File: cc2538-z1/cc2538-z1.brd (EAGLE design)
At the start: 56.8 x 35.6 mm, 61 parts, among them Q2 DMG6602SVT, U1 CC2538, U2 CC1120_RHM_32, U3 TPD2E001IDRLRQ1, U4 CP2103, X1 FA-128, X2 32MHz

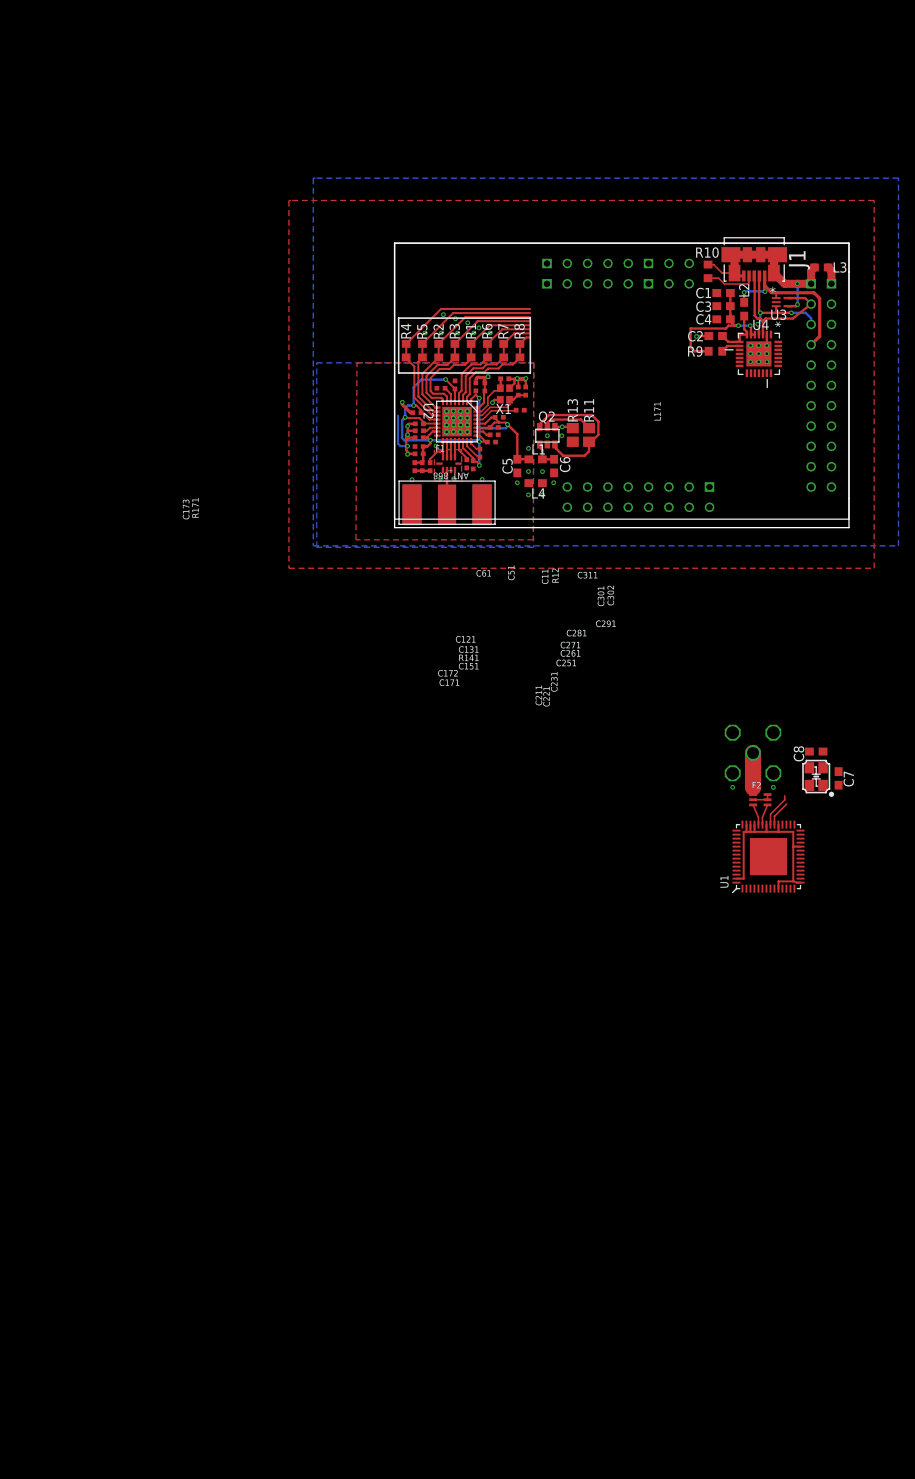
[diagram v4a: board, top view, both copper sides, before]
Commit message: Board check in before placing & routing CPU
Added CC1120/1200 ref chunk

Added partslist with Farnell links
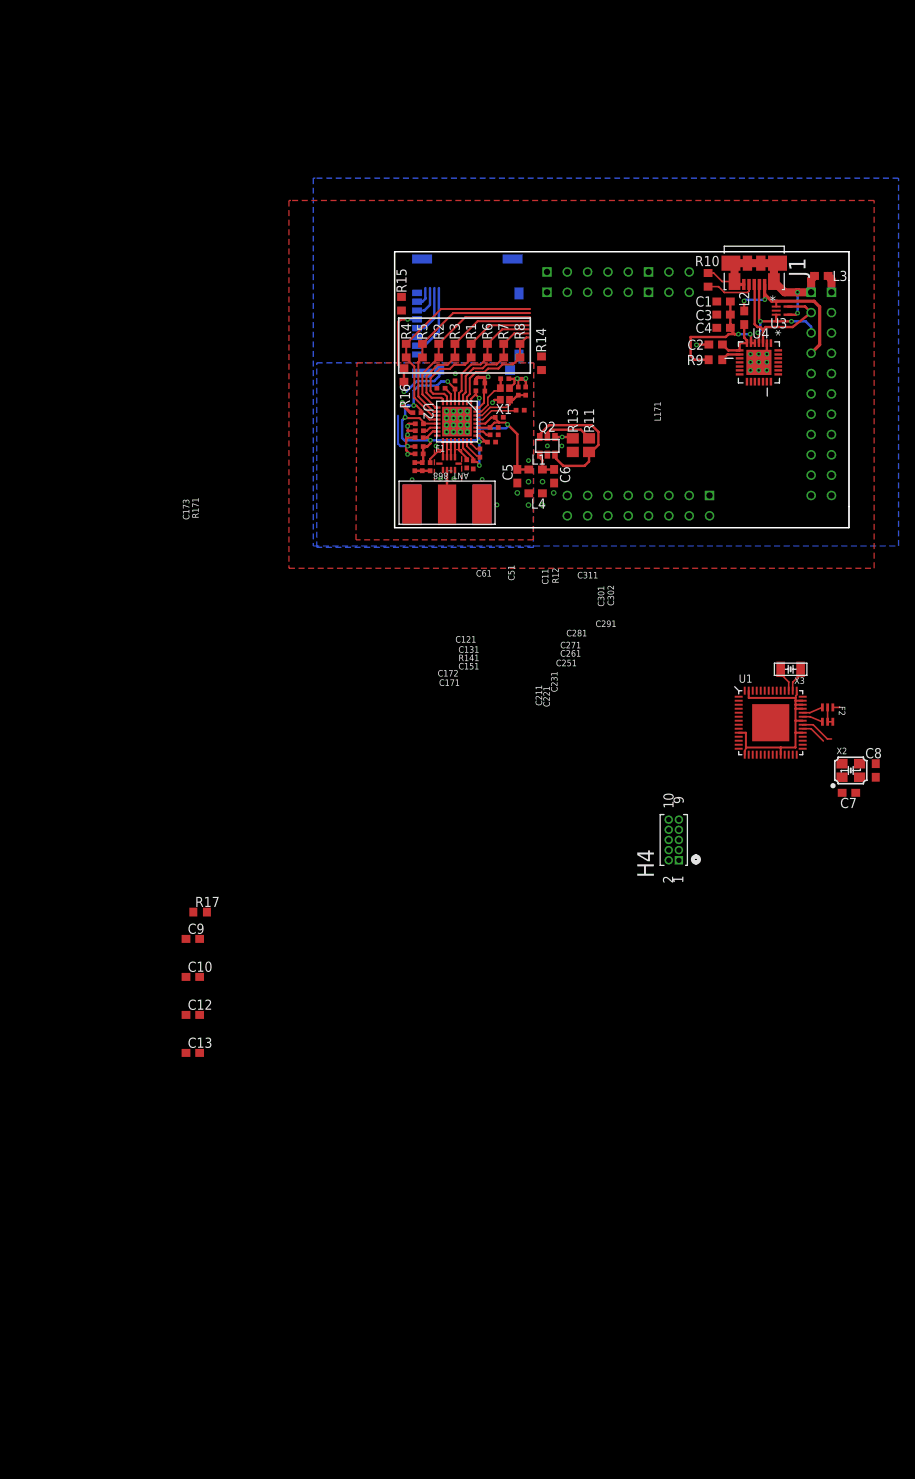
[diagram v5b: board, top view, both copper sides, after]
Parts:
- removed U$1: SMATH, CC11x:SMA
- added C10, C9: 1uF, rcl:C0603
- added C12, C13: 47p, rcl:C0603
- added H4: FTS-105-01-L-D, CC11x:SAMTEC_FTS-105-01-L-D
- added R14: 100k, rcl:R0603
- added R15: DNP, rcl:R0603
- added R16: (no value), rcl:R0603
- added R17: 56k, rcl:R0603
- added SD1: MICRO_SD-SPI-MOLEX_503182-0853, glacsweb:MICRO_SD-MOLEX_503182-0853
- added X3: 32.768K, arm-cores:XTAL-3.2X1.5
- R9: value 4.7k -> 10k
- moved U1 16.7 mm to (47.0, -24.4), turned to 0 degrees
- moved F2 13.6 mm to (54.1, -23.4), turned to 0 degrees
- moved C8 7.81 mm to (60.1, -30.4), turned to 90 degrees
- moved X2 4.38 mm to (57.0, -30.4), turned to 0 degrees
- moved C7 2.22 mm to (56.8, -33.1), turned to 180 degrees
- moved C5 1.27 mm to (15.3, 6.43)
- moved C6 1.27 mm to (19.9, 6.43)
- moved L1 1.27 mm to (17.6, 7.26)
- moved L4 1.27 mm to (17.6, 4.29)
- moved Q2 1.27 mm to (20.4, 9.42)
- moved R11 1.27 mm to (24.3, 10.3)
- moved R13 1.27 mm to (22.3, 10.3)
- moved H1 1.06 mm to (1.27, 34.5)
- moved J1 1.06 mm to (45.0, 30.4)
- moved R10 1.06 mm to (39.2, 31.0)
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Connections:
- removed net ADC_1: H1.A16
- removed net ADC_2: H1.A9
- removed net ADC_BATVOLTS: H1.A6
- removed net I2C_INT: U1.26
- removed net N$22: U1.27
- removed net N$23: U1.20
- removed net N$24: H1.C44
- removed net N$25: H1.C41
- removed net N$32: H1.B29
- removed net N$33: H1.B27
- removed net N$39: H1.A15
- removed net N$42: H1.A5
- removed net N$43: H1.A7
- removed net N$45: H1.A8
- removed net N$49: H1.C52
- removed net N$50: H1.C50
- removed net N$54: H1.C54
- removed net N$56: H1.C45
- removed net N$60: H1.C53
- removed net N$61: H1.C47
- removed net N$69: U1.49
- removed net N$71: U1.48
- new net 32K_Q1: C12.2, U1.45, X3.2
- new net 32K_Q2: C13.2, U1.44, X3.1
- new net ADC_SENSORS_ADC2: H1.A9, U1.20
- new net CC2538_NRESET: H4.10, U1.28
- new net DCOUPL: C10.2, C9.2, U1.32, U1.56
- new net JTAG_TCK: H4.4, U1.47
- new net JTAG_TDI: H4.8
- new net JTAG_TMS: H4.2, H4.6, U1.46
- net +3V3: now also H4.1, R15.2, SD1.DETECT, U1.43
- net 2.4G: no longer U$1.SIG
- net ADC_SENSORS_ADC1: now also H1.A16
- net ADC_SENSORS_ADC3: now also H1.A6
- net DIGITAL_IO_1: now also U1.48
- net DIGITAL_IO_2: now also U1.49
- net GND: now also C10.1, C12.1, C13.1, C9.1, H4.3, H4.5, R14.2, R17.2, SD1.6; no longer U$1.GND1, U$1.GND2, U$1.GND3, U$1.GND4
- net N$21: now also R17.1, U1.42; no longer U1.25
- net PWR_RADIO_EN: now also U1.27
- net PWR_SENSE_EN: now also U1.26
- net RADIO_GPIO2: now also H1.C42
- net RADIO_GPIO3: no longer H1.C42
- net RS485_TXEN: now also U1.25
- net SD_SEL: now also R14.1, R15.1, R16.1, R16.2, SD1.4, SD1.SWITCH
- net SD_SPI_CLK: now also SD1.5
- net SD_SPI_CSN: now also SD1.2
- net SD_SPI_MISO: now also SD1.7
- net SD_SPI_MOSI: now also SD1.3
- net UART0_RX: now also H1.C47
- net UART0_TX: now also H1.C53
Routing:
- net SD_SEL: track 0.00 -> 17.9 mm, vias 0 -> 2
- net SD_SPI_MISO: track 0.00 -> 8.90 mm
- net SD_SPI_CLK: track 0.00 -> 6.46 mm
- net 2.4G: track 5.21 -> 0.86 mm
- net SD_SPI_MOSI: track 0.00 -> 4.01 mm
- net 32K_Q1: track 0.00 -> 3.10 mm
- net 32K_Q2: track 0.00 -> 3.09 mm
- net SD_SPI_CSN: track 0.00 -> 2.53 mm
- net RGND: track 30.1 -> 31.9 mm, vias 18 -> 20
- net RVDD: track 75.8 -> 76.9 mm
- net +3V3: track 34.6 -> 35.6 mm
- net GND: vias 26 -> 15
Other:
- board size 56.8 x 35.6 mm -> 56.8 x 34.5 mm

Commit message: PCB routing attempt 1
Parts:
- added ANT: UFL, CC11x:UFL-HIROSE
- added C14, C15: 1uF, CC11x:C0603
- added J2: 2-PIN-MOLEX, farnell-parts:2-MOLEX
- added LED: (no value), CC11x:PLCC-4_3.2X2.8
- added R18, R19: 100k, rcl:R0603
- added R20, R21, R22: 220, rcl:R0603
- added R23, R24, R25: 4.7K, rcl:R0603
- added R26, R27: 4.7k, rcl:R0603
- added RST, USR: (no value), CC11x:C&K-KMR-5MM
- added U5, U6, U7: BSS138PS, CC11x:SOT65P210X110-6N
- R7: value (none) -> 220
- moved R7 137.6 mm to (-46.0, -101.9), turned to 0 degrees
- moved C13 107.3 mm to (35.6, 22.8), turned to 270 degrees
- moved C12 102.0 mm to (33.2, 22.8), turned to 270 degrees
- moved R17 90.7 mm to (39.3, 16.6)
- moved H4 60.5 mm to (25.3, 23.3), turned to 180 degrees
- moved X2 42.6 mm to (40.5, 8.89)
- moved C7 42.6 mm to (40.3, 6.10)
- moved C8 42.6 mm to (43.6, 8.89)
- moved X3 40.8 mm to (34.4, 20.1)
- moved F2 39.8 mm to (39.0, 13.5)
- moved U1 39.8 mm to (31.9, 12.4)
- moved R11 4.20 mm to (21.3, 13.3), turned to 180 degrees
- moved R8 2.05 mm to (13.6, 21.9)
- moved R14 0.97 mm to (17.5, 20.1), turned to 0 degrees
- moved R9 0.38 mm to (40.1, 21.4)
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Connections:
- removed net DIGITAL_IO_1: H1.C51, U1.48
- removed net DIGITAL_IO_2: H1.A10, U1.49
- removed net JTAG_TDI: H4.8
- new net JTAG_TDI/DIO2: H1.A10, H4.8, U1.49
- new net JTAG_TDO/DIO1: H1.C51, H4.6, U1.48
- new net N$22: LED.1, R20.2
- new net N$23: LED.3, R21.2
- new net N$24: LED.4, R22.2
- new net N$25: R20.1, U5.6
- new net N$32: R21.1, U6.6
- new net N$33: R22.1, U5.3
- net +3V3: now also J2.1, J2.2, LED.2, R18.2, R19.2
- net 2.4G: now also ANT.RF
- net BSL_DTR: now also R27.2, U7.2
- net BSL_RTS: now also R26.2, U7.5
- net CC2538_NRESET: now also C14.1, R18.1, RST.1, RST.5, U7.3
- net GND: now also ANT.1, ANT.2, C14.2, C15.2, H4.9, R23.2, R24.2, R25.2, R26.1, R27.1, RST.2, RST.3, RST.4, U5.1, U5.4, U6.1, U7.1, U7.4, USR.2, USR.3, USR.4
- net JTAG_TMS: no longer H4.6
- net LEDS_BLUE: now also R25.1, U6.2
- net LEDS_GREEN: now also R24.1, U5.5
- net LEDS_RED: now also R23.1, U5.2
- net RADIO_GPIO3: no longer R7.1, R7.2
- net USER_BUTTON: now also C15.1, R19.1, U7.6, USR.1, USR.5
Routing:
- net UART0_TX: track 0.00 -> 52.5 mm, vias 0 -> 3
- net UART0_RX: track 0.00 -> 46.3 mm, vias 0 -> 2
- net USER_BUTTON: track 0.00 -> 38.8 mm
- net CC2538_NRESET: track 0.00 -> 23.2 mm
- net RADIO_SPI_CSN: track 28.2 -> 49.7 mm, vias 0 -> 1
- net RADIO_GPIO0: track 25.0 -> 45.6 mm, vias 0 -> 1
- net RADIO_SPI_MISO: track 22.8 -> 42.8 mm, vias 0 -> 1
- net RADIO_SPI_CLK: track 21.6 -> 40.9 mm, vias 0 -> 1
- net RADIO_RESET_N: track 13.7 -> 33.0 mm
- net RADIO_SPI_MOSI: track 20.9 -> 39.6 mm, vias 0 -> 1
- net RADIO_GPIO2: track 15.5 -> 34.0 mm
- net SD_SPI_CSN: track 2.53 -> 20.8 mm
- net SD_SPI_MOSI: track 4.01 -> 20.7 mm
- net BSL_DTR: track 0.00 -> 16.6 mm, vias 0 -> 2
- net RADIO_GPIO3: track 14.6 -> 0.00 mm
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
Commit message: 48 airwires left.
Still need to finalise SD sel setup.

May need to swap to a 4-layer board.

What am I doing working on PCBs at 8 am?
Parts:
- removed R7: 220, rcl:R0603
- moved R19 102.7 mm to (43.2, -2.29)
- moved R18 92.4 mm to (54.8, 1.45)
- moved C10 89.7 mm to (24.8, 18.3)
- moved C9 84.6 mm to (36.4, 6.53), turned to 90 degrees
- moved R25 42.9 mm to (-23.6, -79.8), turned to 180 degrees
- moved R24 35.2 mm to (-23.6, -84.3), turned to 180 degrees
- moved R23 33.3 mm to (-23.6, -82.0), turned to 180 degrees
- moved X3 2.30 mm to (34.1, 22.4)
- moved C12 2.30 mm to (32.9, 25.0)
- moved C13 2.30 mm to (35.4, 25.0)
- moved C8 1.80 mm to (42.4, 10.2)
- moved F2 1.80 mm to (37.7, 14.7)
- moved R17 1.80 mm to (38.0, 17.9)
- moved U1 1.80 mm to (30.6, 13.7)
- moved ANT 1.80 mm to (41.3, 15.6)
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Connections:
- net RADIO_GPIO0: now also H1.C54
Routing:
- net PWR_RADIO_EN: track 2.90 -> 49.7 mm, vias 1 -> 3
- net RADIO_SPI_MISO: track 42.8 -> 86.8 mm, vias 1 -> 2
- net RADIO_SPI_MOSI: track 39.6 -> 78.4 mm, vias 1 -> 2
- net I2C_SCL: track 0.00 -> 37.4 mm, vias 0 -> 2
- net I2C_SDA: track 0.00 -> 37.1 mm, vias 0 -> 2
- net RADIO_SPI_CLK: track 40.9 -> 75.1 mm, vias 1 -> 2
- net PWR_SENSE_EN: track 0.00 -> 31.4 mm, vias 0 -> 2
- net UART1_RX: track 0.00 -> 30.3 mm, vias 0 -> 1
- net UART1_TX: track 0.00 -> 27.6 mm, vias 0 -> 1
- net DCOUPL: track 0.00 -> 24.1 mm, vias 0 -> 2
- net SD_SPI_CLK: track 20.9 -> 43.8 mm, vias 0 -> 1
- net SD_SPI_MOSI: track 20.7 -> 42.1 mm, vias 0 -> 1
- net SD_SPI_MISO: track 22.6 -> 43.5 mm, vias 0 -> 1
- net JTAG_TCK: track 0.00 -> 8.13 mm
- net JTAG_TMS: track 0.00 -> 7.29 mm
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
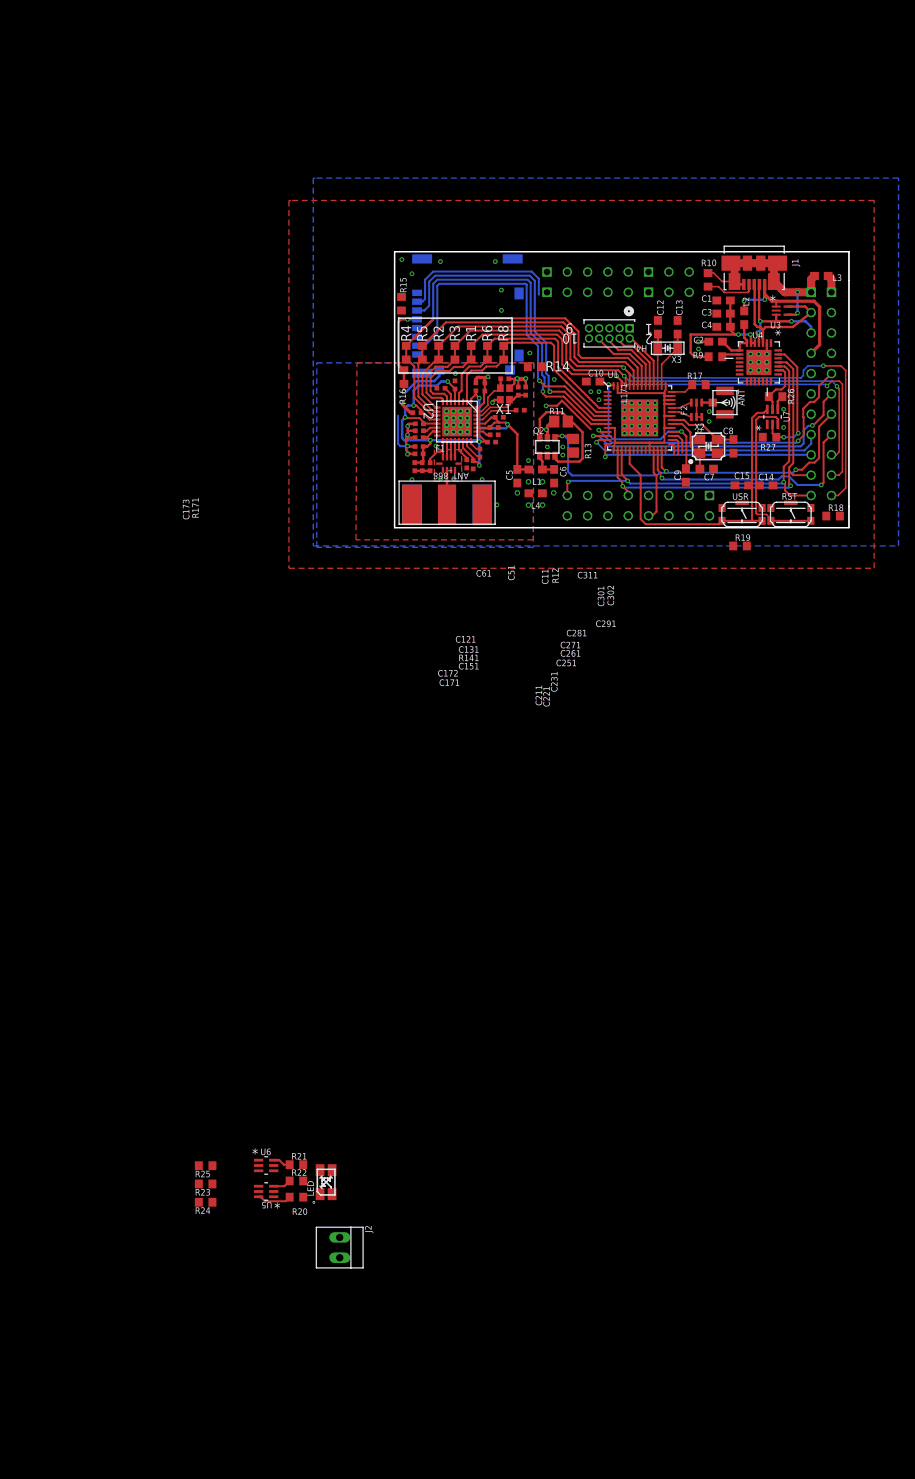
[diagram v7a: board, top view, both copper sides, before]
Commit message: Last commit before going 4-layer for cc2538 board.
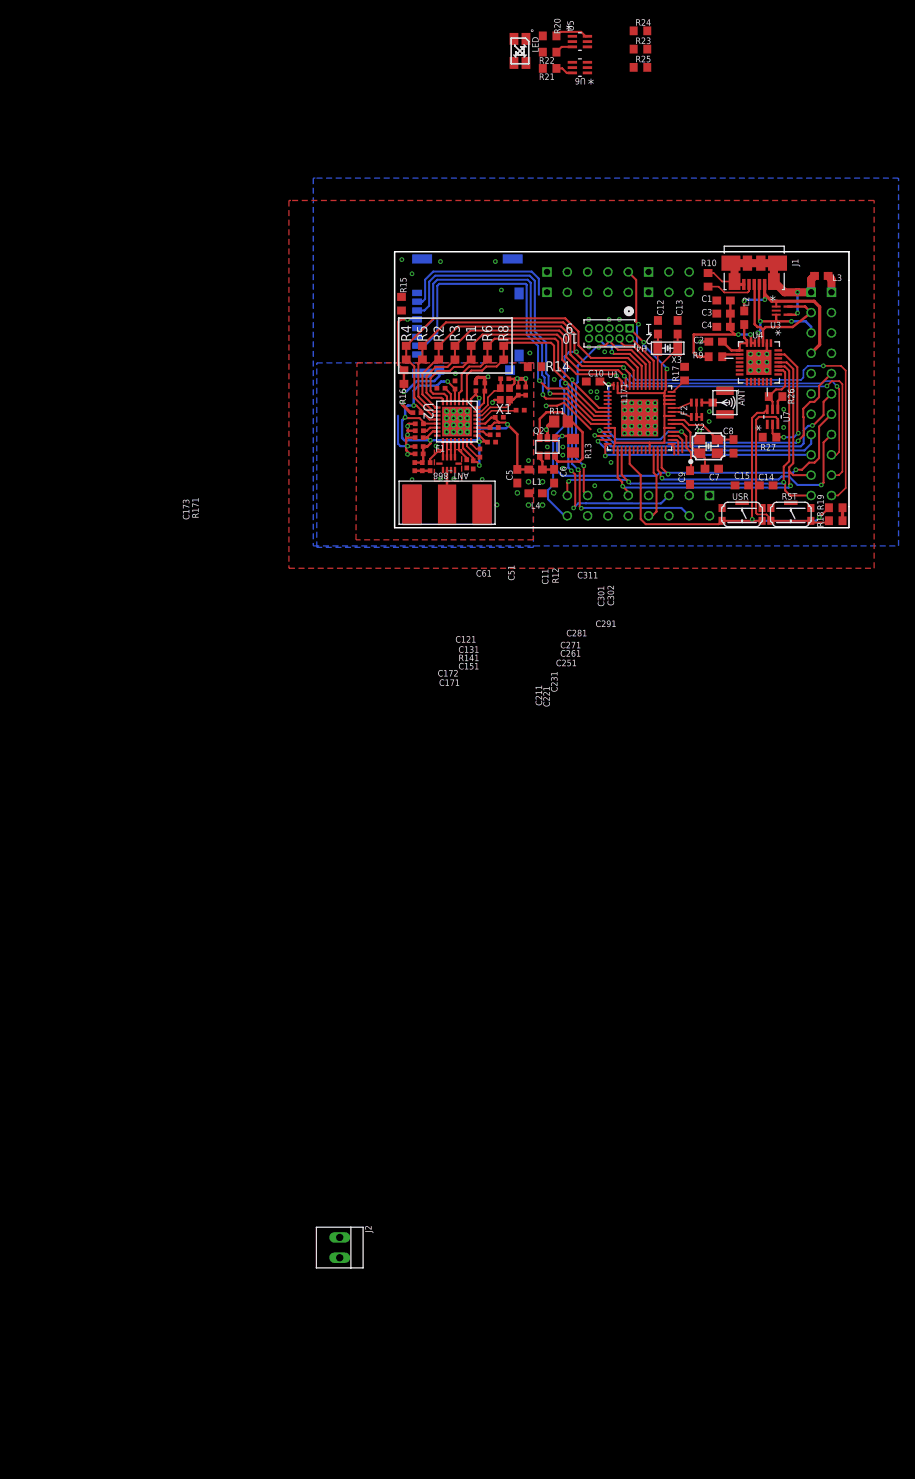
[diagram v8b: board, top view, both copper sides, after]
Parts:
- moved R24 156.2 mm to (30.7, 62.1), turned to 0 degrees
- moved R23 151.9 mm to (30.7, 59.8), turned to 0 degrees
- moved U5 149.0 mm to (23.2, 60.8), turned to 0 degrees
- moved R20 148.6 mm to (19.4, 61.5), turned to 180 degrees
- moved R25 147.7 mm to (30.7, 57.5), turned to 0 degrees
- moved R22 144.6 mm to (19.4, 59.4), turned to 180 degrees
- moved LED 143.5 mm to (15.7, 59.6), turned to 180 degrees
- moved U6 142.7 mm to (23.2, 57.5), turned to 180 degrees
- moved R21 140.6 mm to (19.4, 57.4), turned to 180 degrees
- moved R19 12.9 mm to (55.1, 2.49)
- moved R17 2.28 mm to (36.2, 19.3), turned to 90 degrees
- moved R18 0.67 mm to (55.1, 0.86)
- moved C7 0.63 mm to (39.6, 7.37)
- moved C9 0.57 mm to (36.9, 6.27)
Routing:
- net RADIO_GPIO2: track 30.2 -> 60.9 mm, vias 0 -> 3
- net RADIO_RESET_N: track 29.3 -> 58.4 mm, vias 0 -> 3
- net RADIO_GPIO0: track 43.6 -> 67.6 mm, vias 0 -> 1
- net JTAG_TDO/DIO1: track 8.78 -> 31.3 mm, vias 0 -> 2
- net JTAG_TDI/DIO2: track 9.30 -> 22.6 mm, vias 0 -> 2
- net +3V3: track 33.2 -> 44.1 mm, vias 1 -> 3
- net USER_BUTTON: track 40.6 -> 51.1 mm, vias 0 -> 2
- net CC2538_NRESET: track 23.2 -> 25.9 mm
- net PWR_RADIO_EN: track 49.7 -> 51.3 mm
- net GND: track 28.0 -> 27.3 mm, vias 59 -> 67
- net +3V3_SERIAL: track 18.7 -> 17.9 mm
- net RADIO_SPI_CSN: track 47.8 -> 47.2 mm
- net N$21: track 2.94 -> 2.36 mm
- net I2C_SDA: track 37.1 -> 36.6 mm
